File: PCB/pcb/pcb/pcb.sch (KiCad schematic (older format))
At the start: 5 parts, among them P1 Conn_02x20_Odd_Even

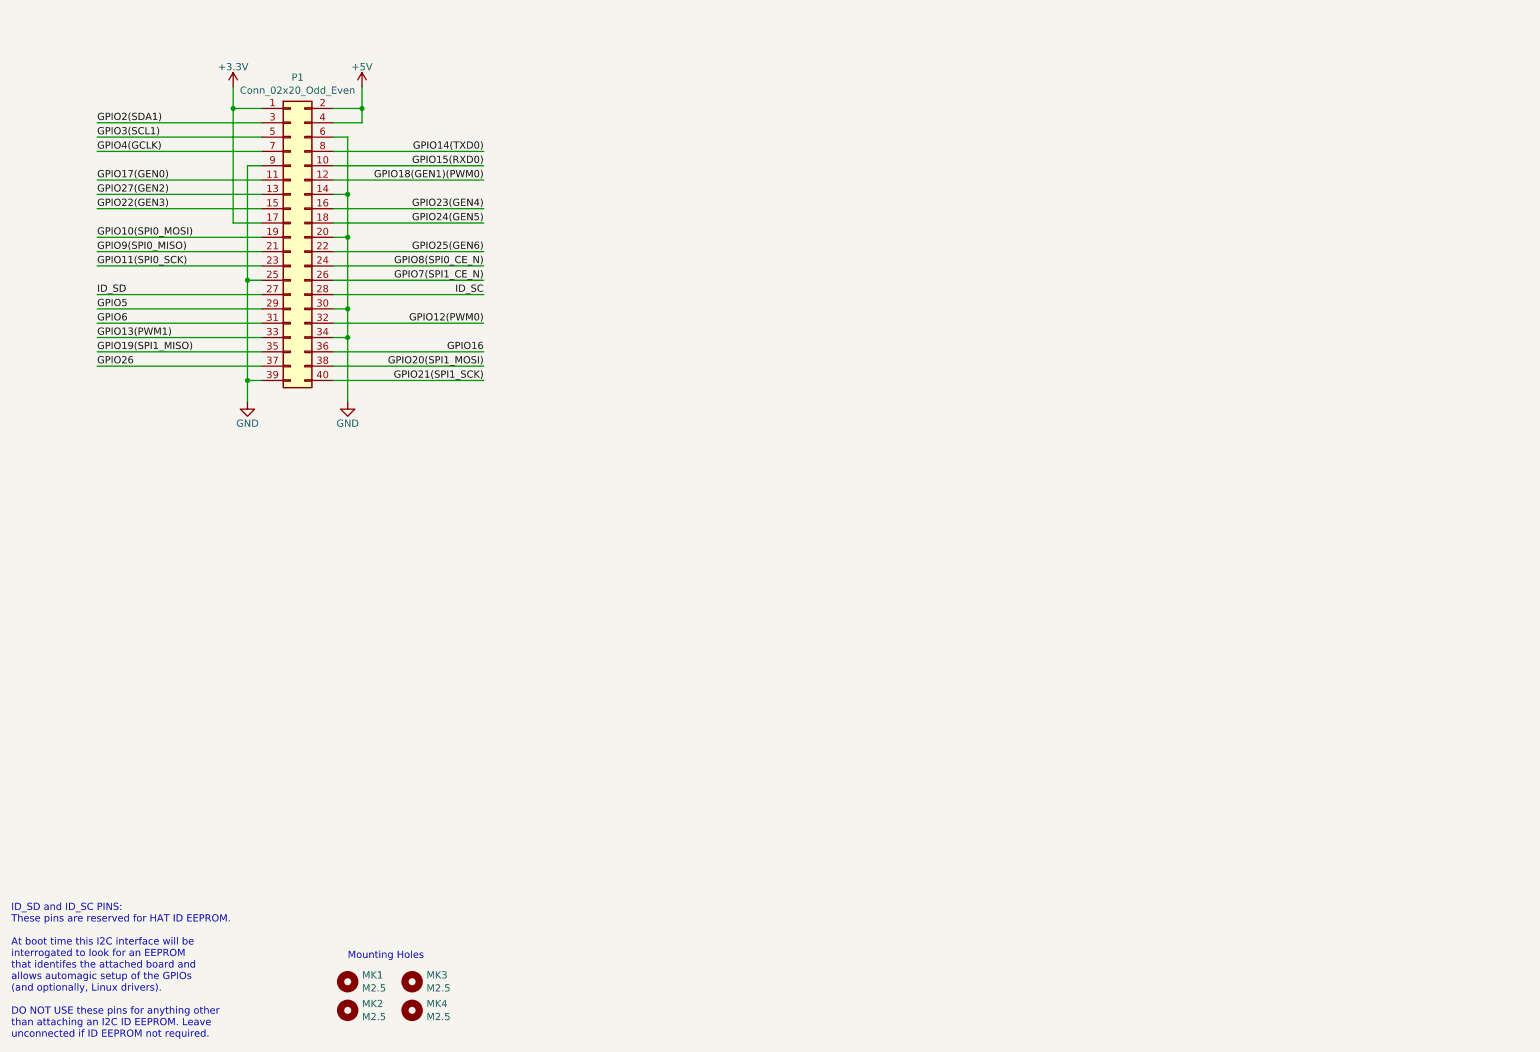
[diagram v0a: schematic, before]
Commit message: v0.6 drivers symbols created
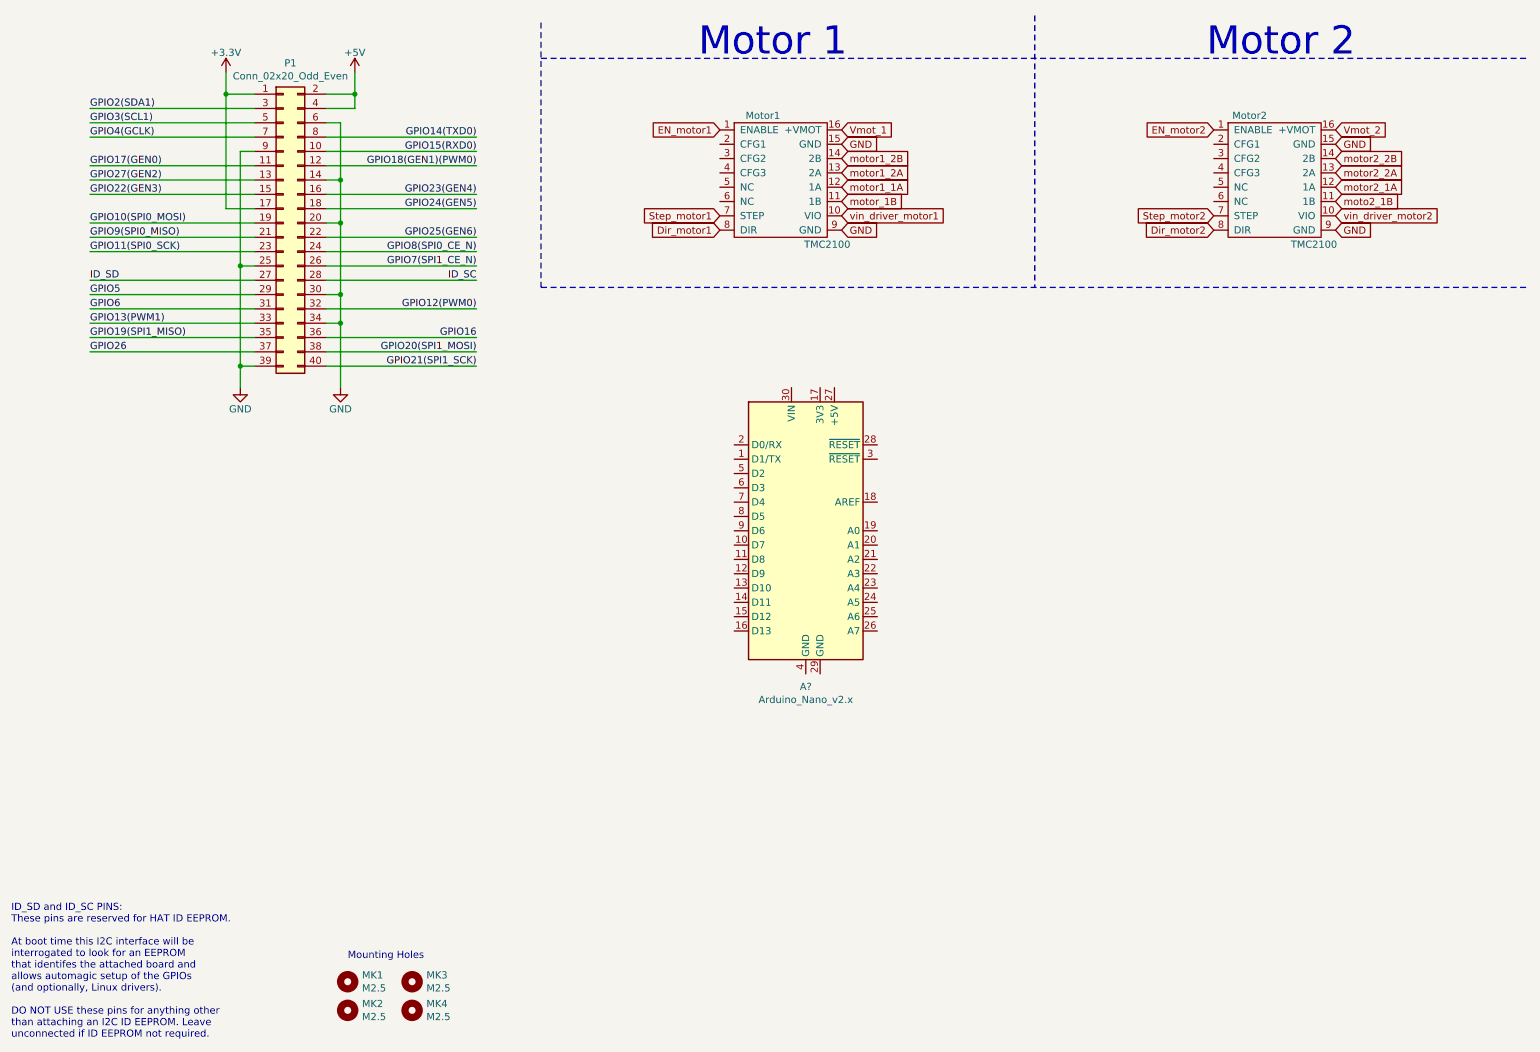
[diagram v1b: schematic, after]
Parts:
- added A?: Arduino_Nano_v2.x, Module:Arduino_Nano, symbol MCU_Module:Arduino_Nano_v2.x
- added Motor1, Motor2: TMC2100, symbol Drivers:TMC2100
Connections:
- net GND: now also Motor1.15 (GND), Motor1.9 (GND), Motor2.15 (GND), Motor2.9 (GND)
- new net Dir_motor1: Motor1.8 (DIR)
- new net Dir_motor2: Motor2.8 (DIR)
- new net EN_motor1: Motor1.1 (ENABLE)
- new net EN_motor2: Motor2.1 (ENABLE)
- new net Step_motor1: Motor1.7 (STEP)
- new net Step_motor2: Motor2.7 (STEP)
- new net Vmot_1: Motor1.16 (+VMOT)
- new net Vmot_2: Motor2.16 (+VMOT)
- new net moto2_1B: Motor2.11 (1B)
- new net motor1_1A: Motor1.12 (1A)
- new net motor1_2A: Motor1.13 (2A)
- new net motor1_2B: Motor1.14 (2B)
- new net motor2_1A: Motor2.12 (1A)
- new net motor2_2A: Motor2.13 (2A)
- new net motor2_2B: Motor2.14 (2B)
- new net motor_1B: Motor1.11 (1B)
- new net vin_driver_motor1: Motor1.10 (VIO)
- new net vin_driver_motor2: Motor2.10 (VIO)
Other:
- note added: "Motor 1\n"
- note added: "Motor 2\n"
- moved on the sheet: P1
